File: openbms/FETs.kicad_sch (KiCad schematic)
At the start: 29 parts, among them Q1 NTMFS5C612NLT1G, Q2 NTMFS5C612NLT1G, Q3 BSS84AKW,115, Q4 2N7002KW, Q5 2N7002KW, U18 DMP68D1LVQ-7, U19 TPS12000QDGXRQ1

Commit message: Footprints for pmos/nmos and pmos/pmos packages fixed, charger detection added, pwr_gd and flt_gd lines removed
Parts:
- added C44: 10n, Capacitor_SMD:C_0402_1005Metric, symbol Device:C_Small
- added D15: BAT54J, Diode_SMD:D_SOD-323F, symbol Diode:BAT54J
- added R116: 100k, Resistor_SMD:R_0402_1005Metric, symbol Device:R_Small
- added R118: 10k, Resistor_SMD:R_0402_1005Metric, symbol Device:R_Small
- Q1, Q2: footprint custom_library:ONSemi_SO-8FL_488AA -> Package_SO:ONSemi_SO-8FL_488AA
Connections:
- net +3V3: now also D15.1 (K)
- net GND: now also C44.2, R118.2
- net SYS_VCC: now also R116.1
- net DRV_FLT_GD: no longer names the net of U19.4 (FLT_GD)
- new net CHG_PRES: C44.1, D15.2 (A), R116.2, R118.1
- no-connect marks 0 -> 1
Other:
- moved on the sheet: D7, Q4, R90, R91, R93, R96, U18

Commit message: Button for quick enable added
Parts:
- Q1, Q2: footprint Package_SO:ONSemi_SO-8FL_488AA -> custom_library:ONSemi_SO-8FL_488AA
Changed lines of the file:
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@@
 			)
 		)
-		(property "Footprint" "Package_SO:ONSemi_SO-8FL_488AA"
+		(property "Footprint" "custom_library:ONSemi_SO-8FL_488AA"
 			(at 158.115 96.52 0)
 			(effects
@@
 			)
 		)
-		(property "Footprint" "Package_SO:ONSemi_SO-8FL_488AA"
+		(property "Footprint" "custom_library:ONSemi_SO-8FL_488AA"
 			(at 173.355 96.52 0)
 			(effects

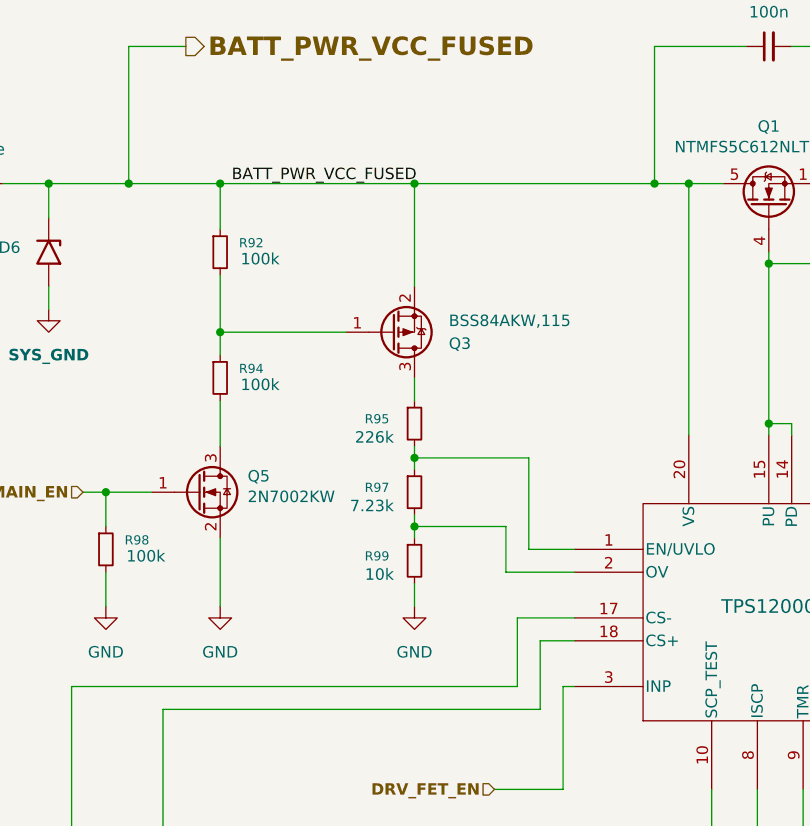
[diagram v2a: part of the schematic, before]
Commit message: FET driver EN and OV pin voltage levels fixed
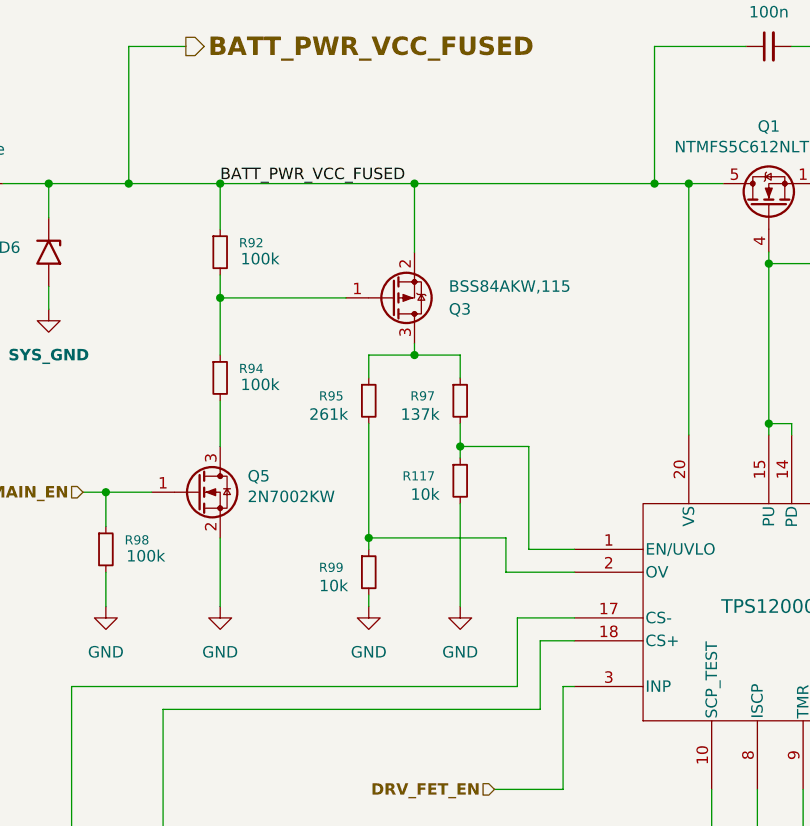
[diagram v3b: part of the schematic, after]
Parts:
- added R117: 10k, Resistor_SMD:R_0402_1005Metric, symbol Device:R_Small
- R95: value 226k -> 261k; Manufacturer_Part_Number RN73R1ETTP2263B25 -> RC0402FR-07261KL
- R97: value 7.23k -> 137k; Manufacturer_Part_Number RN73R1ETTP7231B25 -> RC0402FR-07137KL
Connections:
- net GND: now also R117.2
- net at R99.1, U19.2 (OV): now also R95.2; no longer R97.2
- net at Q3.3 (D), R95.1: now also R97.1
- new net: R117.1, R97.2, U19.1 (EN/UVLO)
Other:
- moved on the sheet: Q3, R95, R99

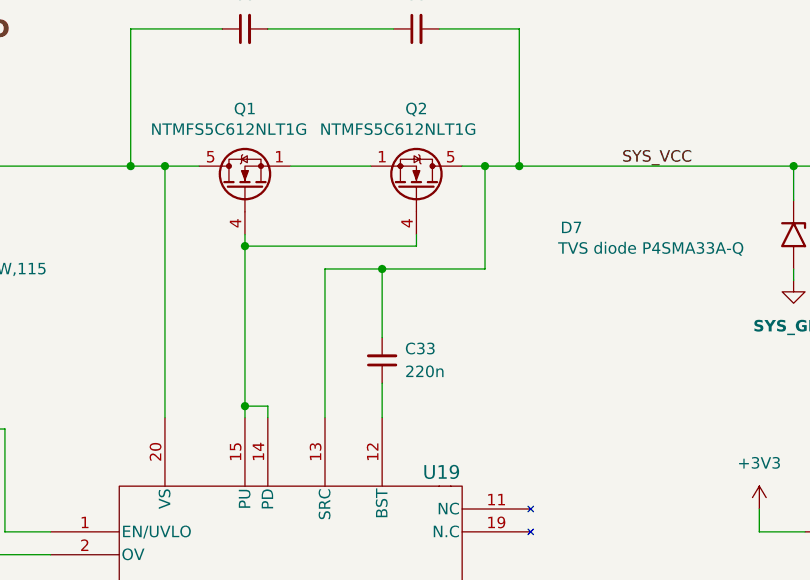
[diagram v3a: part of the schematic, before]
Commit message: Polygon zone fixed, SRC net in FET fixed
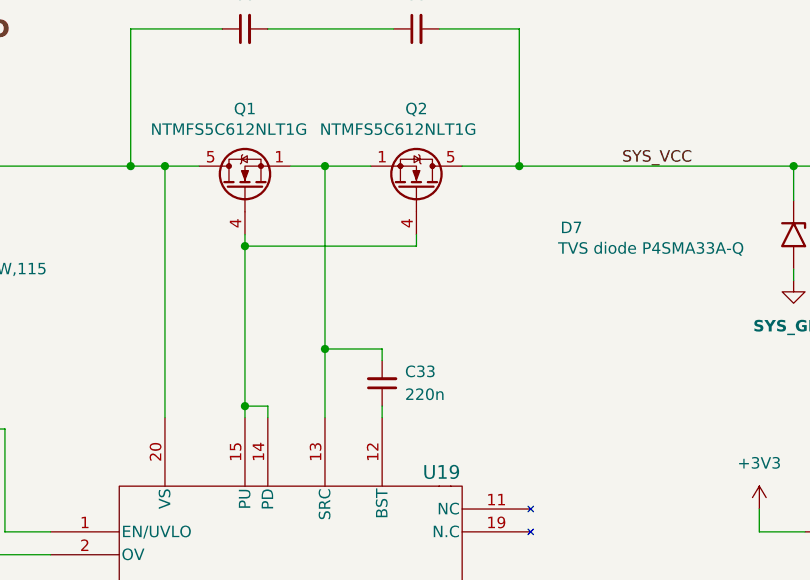
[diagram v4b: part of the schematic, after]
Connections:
- net SYS_VCC: no longer C33.2, U19.13 (SRC)
- net at Q1.1 (S), Q1.2 (S), Q1.3 (S)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: now also C33.2, U19.13 (SRC)
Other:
- moved on the sheet: C33
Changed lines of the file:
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@@
 	)
 	(junction
+		(at 165.1 99.06)
+		(diameter 0)
+		(color 0 0 0 0)
+	)
+	(junction
 		(at 85.09 99.06)
 		(diameter 0)
@@
 	)
 	(junction
+		(at 165.1 119.38)
+		(diameter 0)
+		(color 0 0 0 0)
+	)
+	(junction
 		(at 121.92 128.27)
 		(diameter 0)
@@
 	)
 	(junction
-		(at 171.45 110.49)
-		(diameter 0)
-		(color 0 0 0 0)
-	)
-	(junction
-		(at 182.88 99.06)
-		(diameter 0)
-		(color 0 0 0 0)
-	)
-	(junction
 		(at 116.84 99.06)
 		(diameter 0)
@@
 	(wire
 		(pts
-			(xy 182.88 99.06) (xy 186.69 99.06)
+			(xy 218.44 139.7) (xy 213.36 139.7)
 		)
 		(stroke
@@
 	(wire
 		(pts
-			(xy 218.44 139.7) (xy 213.36 139.7)
+			(xy 46.99 99.06) (xy 63.5 99.06)
 		)
 		(stroke
@@
 	(wire
 		(pts
-			(xy 46.99 99.06) (xy 63.5 99.06)
+			(xy 320.04 134.62) (xy 320.04 137.16)
 		)
 		(stroke
@@
 	(wire
 		(pts
-			(xy 320.04 134.62) (xy 320.04 137.16)
+			(xy 214.63 212.09) (xy 214.63 215.9)
 		)
 		(stroke
@@
 	(wire
 		(pts
-			(xy 214.63 212.09) (xy 214.63 215.9)
+			(xy 128.27 154.94) (xy 128.27 147.32)
 		)
 		(stroke
@@
 	(wire
 		(pts
-			(xy 128.27 154.94) (xy 128.27 147.32)
+			(xy 165.1 99.06) (xy 165.1 119.38)
 		)
 		(stroke
@@
 	(wire
 		(pts
-			(xy 165.1 110.49) (xy 171.45 110.49)
+			(xy 233.68 139.7) (xy 240.03 139.7)
 		)
 		(stroke
@@
 	(wire
 		(pts
-			(xy 233.68 139.7) (xy 240.03 139.7)
+			(xy 170.18 185.42) (xy 170.18 181.61)
 		)
 		(stroke
@@
 	(wire
 		(pts
-			(xy 170.18 185.42) (xy 170.18 181.61)
+			(xy 214.63 212.09) (xy 227.33 212.09)
 		)
 		(stroke
@@
 	(wire
 		(pts
-			(xy 214.63 212.09) (xy 227.33 212.09)
+			(xy 213.36 137.16) (xy 213.36 139.7)
 		)
 		(stroke
@@
 	(wire
 		(pts
-			(xy 213.36 137.16) (xy 213.36 139.7)
+			(xy 171.45 120.65) (xy 171.45 119.38)
 		)
 		(stroke
@@
 	(wire
 		(pts
-			(xy 161.29 99.06) (xy 170.18 99.06)
+			(xy 161.29 99.06) (xy 165.1 99.06)
 		)
 		(stroke
@@
 	(wire
 		(pts
-			(xy 182.88 110.49) (xy 182.88 99.06)
+			(xy 87.63 212.09) (xy 88.9 212.09)
 		)
 		(stroke
@@
 	(wire
 		(pts
-			(xy 87.63 212.09) (xy 88.9 212.09)
+			(xy 147.32 193.04) (xy 147.32 190.5)
 		)
 		(stroke
@@
 	(wire
 		(pts
-			(xy 147.32 193.04) (xy 147.32 190.5)
+			(xy 78.74 212.09) (xy 78.74 220.98)
 		)
 		(stroke
@@
 	(wire
 		(pts
-			(xy 78.74 212.09) (xy 78.74 220.98)
+			(xy 165.1 99.06) (xy 170.18 99.06)
 		)
 		(stroke
@@
 	(wire
 		(pts
-			(xy 171.45 110.49) (xy 182.88 110.49)
+			(xy 129.54 139.7) (xy 134.62 139.7)
 		)
 		(stroke
@@
 	(wire
 		(pts
-			(xy 129.54 139.7) (xy 134.62 139.7)
+			(xy 233.68 149.86) (xy 233.68 147.32)
 		)
 		(stroke
@@
 	(wire
 		(pts
-			(xy 233.68 149.86) (xy 233.68 147.32)
+			(xy 88.9 220.98) (xy 88.9 212.09)
 		)
 		(stroke
@@
 	(wire
 		(pts
-			(xy 88.9 220.98) (xy 88.9 212.09)
+			(xy 95.25 111.76) (xy 95.25 109.22)
 		)
 		(stroke
@@
 	(wire
 		(pts
-			(xy 95.25 111.76) (xy 95.25 109.22)
+			(xy 147.32 99.06) (xy 147.32 127)
 		)
 		(stroke
@@
 	(wire
 		(pts
-			(xy 147.32 99.06) (xy 147.32 127)
+			(xy 133.35 166.37) (xy 133.35 154.94)
 		)
 		(stroke
@@
 	(wire
 		(pts
-			(xy 133.35 166.37) (xy 133.35 154.94)
+			(xy 165.1 119.38) (xy 165.1 127)
 		)
 		(stroke
@@
 	(wire
 		(pts
-			(xy 182.88 99.06) (xy 180.34 99.06)
-		)
-		(stroke
-			(width 0)
-			(type default)
-		)
-	)
-	(wire
-		(pts
-			(xy 165.1 127) (xy 165.1 110.49)
+			(xy 180.34 99.06) (xy 186.69 99.06)
 		)
 		(stroke
@@
 	(wire
 		(pts
-			(xy 171.45 123.19) (xy 171.45 127)
+			(xy 171.45 125.73) (xy 171.45 127)
 		)
 		(stroke
@@
 	(wire
 		(pts
-			(xy 171.45 110.49) (xy 171.45 118.11)
+			(xy 186.69 99.06) (xy 217.17 99.06)
 		)
 		(stroke
@@
 	(wire
 		(pts
-			(xy 186.69 99.06) (xy 217.17 99.06)
+			(xy 82.55 146.05) (xy 82.55 142.24)
 		)
 		(stroke
@@
 	(wire
 		(pts
-			(xy 82.55 146.05) (xy 82.55 142.24)
+			(xy 171.45 119.38) (xy 165.1 119.38)
 		)
 		(stroke
@@
 	(symbol
 		(lib_id "Device:C_Small")
-		(at 171.45 120.65 180)
+		(at 171.45 123.19 180)
 		(unit 1)
 		(exclude_from_sim no)
@@
 		(fields_autoplaced yes)
 		(property "Reference" "C33"
-			(at 173.99 119.3735 0)
+			(at 173.99 121.9135 0)
 			(effects
 				(font
@@
 		)
 		(property "Value" "220n"
-			(at 173.99 121.9135 0)
+			(at 173.99 124.4535 0)
 			(effects
 				(font
@@
 		)
 		(property "Footprint" "Capacitor_SMD:C_0603_1608Metric"
-			(at 171.45 120.65 0)
+			(at 171.45 123.19 0)
 			(effects
 				(font
@@
 		)
 		(property "Datasheet" "~"
-			(at 171.45 120.65 0)
+			(at 171.45 123.19 0)
 			(effects
 				(font
@@
 		)
 		(property "Description" "Unpolarized capacitor, small symbol"
-			(at 171.45 120.65 0)
+			(at 171.45 123.19 0)
 			(effects
 				(font
@@
 		)
 		(property "Package" "0603"
-			(at 171.45 120.65 0)
+			(at 171.45 123.19 0)
 			(effects
 				(font
@@
 		)
 		(property "Manufacturer_Part_Number" "CL10E224KA84PNC"
-			(at 171.45 120.65 0)
+			(at 171.45 123.19 0)
 			(effects
 				(font
@@
 		)
 		(property "Pakcage" ""
-			(at 171.45 120.65 0)
+			(at 171.45 123.19 0)
 			(effects
 				(font

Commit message: D15 diode parameters updated, BOM updated
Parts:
- D15: Manufacturer_Part_Number (none) -> BAT54J; Package (none) -> SOD-323
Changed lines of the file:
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@@
+			)
+		)
+		(property "Package" "SOD-323"
+			(at 222.25 139.7 0)
+			(effects
+				(font
+					(size 1.27 1.27)
+				)
+				(hide yes)
+			)
+		)
+		(property "Manufacturer_Part_Number" "BAT54J"
+			(at 222.25 139.7 0)
+			(effects
+				(font
+					(size 1.27 1.27)
+				)
+				(hide yes)
 			)
 		)
